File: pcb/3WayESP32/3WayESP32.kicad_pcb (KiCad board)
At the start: 2 copper layers, 30.8 x 32 mm, 8 parts, among them J1 Conn_01x06_Pin, J2 Conn_01x06_Pin, J3 Conn_01x06_Pin

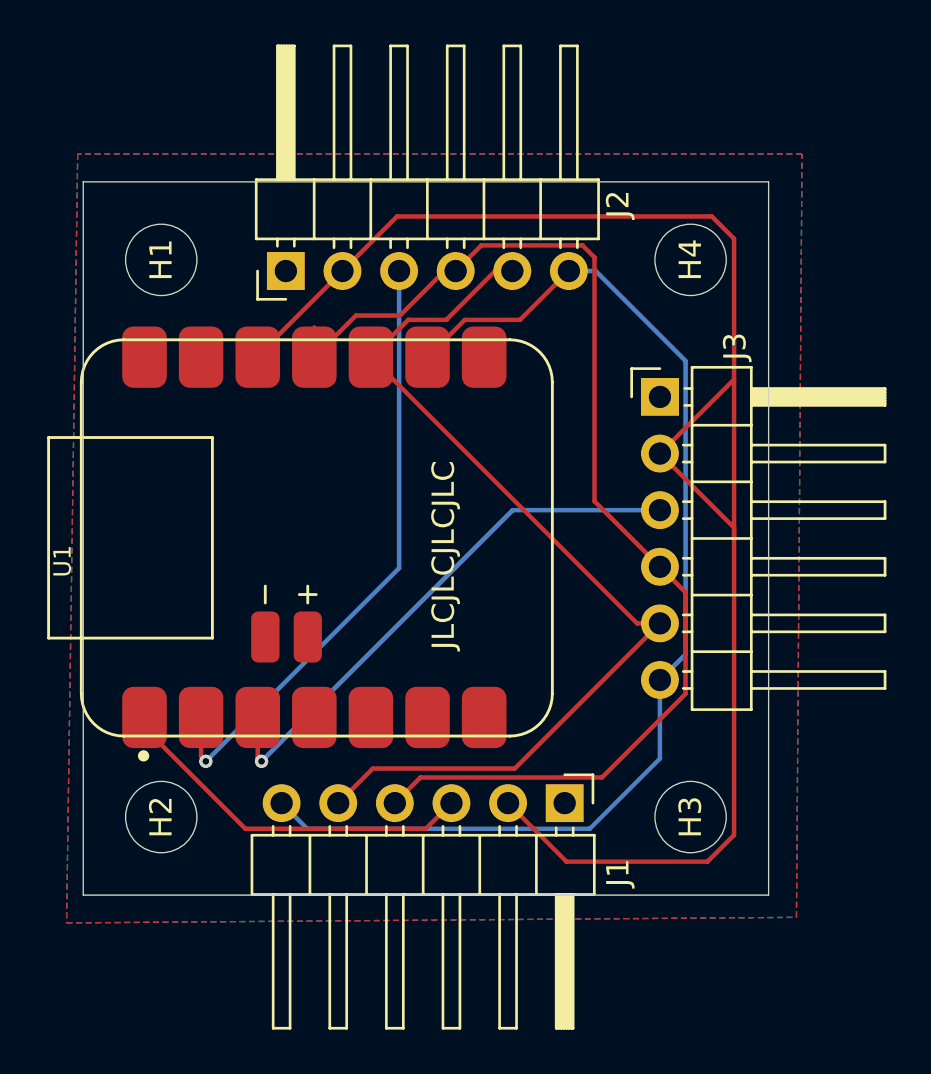
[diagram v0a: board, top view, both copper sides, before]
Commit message: Plated mounting holes
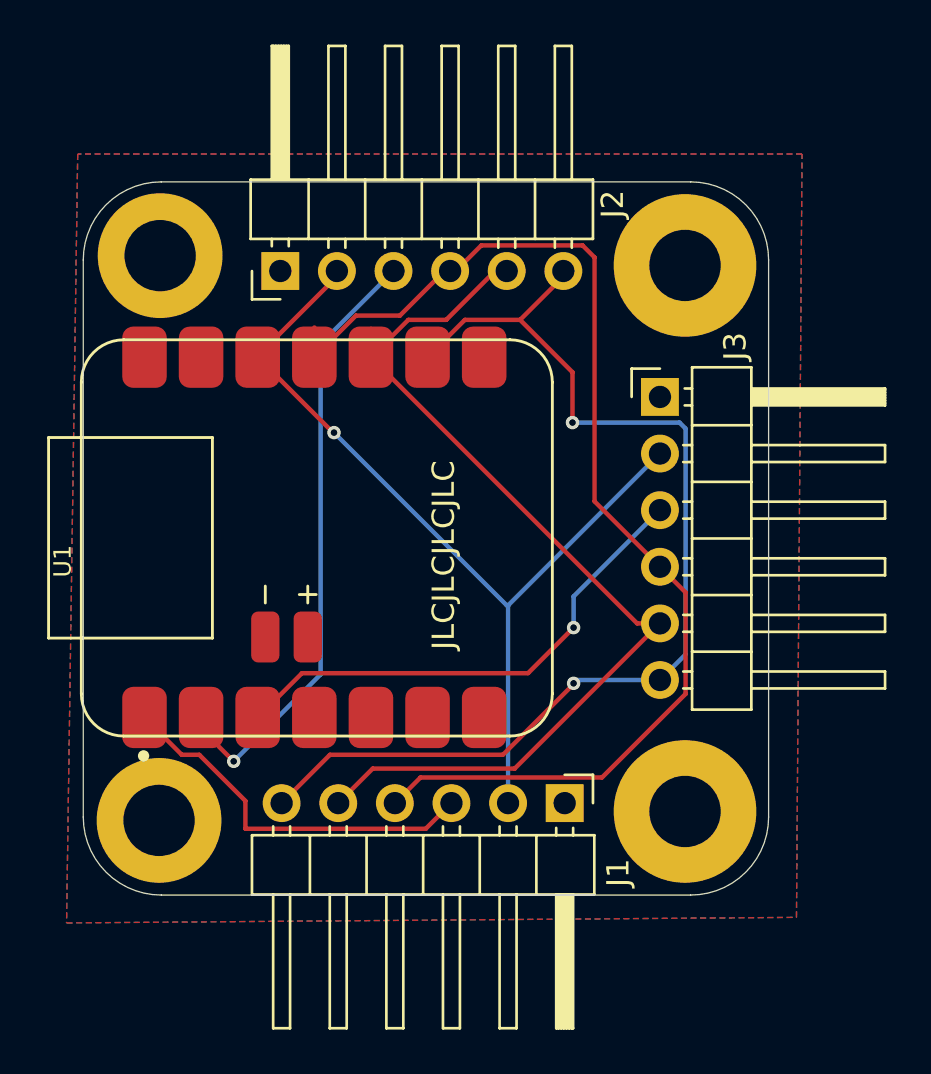
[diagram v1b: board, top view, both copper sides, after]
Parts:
- H1, H2: value MountingHole -> MountingHole_Pad; footprint MountingHole:MountingHole_3.2mm_M3 -> MountingHole:MountingHole_3.2mm_M3_DIN965_Pad
- H3, H4: value MountingHole -> MountingHole_Pad; footprint MountingHole:MountingHole_3.2mm_M3 -> MountingHole:MountingHole_3.2mm_M3_Pad
- moved H2 25.2 mm to (149.2, 90.3), turned to 0 degrees
- moved H1 25.2 mm to (149.2, 115.7), turned to 0 degrees
- moved H3 0.35 mm to (172.8, 115.2), turned to 0 degrees
- moved H4 0.35 mm to (172.8, 90.8), turned to 0 degrees
- moved J2 0.25 mm to (154.6, 91.0)
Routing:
- net +3V3: track 72.8 -> 40.0 mm, vias 0 -> 1
- net /SCK: track 51.9 -> 49.7 mm, vias 0 -> 2
- net /SS3: track 24.6 -> 22.7 mm
- net /SS1: track 16.6 -> 17.5 mm
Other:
- outline, holes or cut-outs redrawn
